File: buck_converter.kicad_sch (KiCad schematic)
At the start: 19 parts, among them Q5 CSD17579Q3A, Q6 CSD17579Q3A, U5 TPS40305DRCR

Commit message: some new ideas for power
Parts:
- removed C47, C53: 1uF, Capacitor_SMD:C_0603_1608Metric_Pad1.08x0.95mm_HandSolder, symbol Device:C
- removed C48: 4.7uF, Capacitor_SMD:C_0603_1608Metric_Pad1.08x0.95mm_HandSolder, symbol Device:C
- removed C49: 3.3nF, Capacitor_SMD:C_0603_1608Metric_Pad1.08x0.95mm_HandSolder, symbol Device:C
- removed C50: 3.9nF, Capacitor_SMD:C_0603_1608Metric_Pad1.08x0.95mm_HandSolder, symbol Device:C
- removed C51: 100pF, Capacitor_SMD:C_0603_1608Metric_Pad1.08x0.95mm_HandSolder, symbol Device:C
- removed C52: 100nF, Capacitor_SMD:C_0603_1608Metric_Pad1.08x0.95mm_HandSolder, symbol Device:C
- removed C54: 1nF, Capacitor_SMD:C_0603_1608Metric_Pad1.08x0.95mm_HandSolder, symbol Device:C
- removed C55: 100uF, Capacitor_SMD:C_0603_1608Metric_Pad1.08x0.95mm_HandSolder, symbol Device:C
- removed L1: XAL7070-182MEC, INDC7275X700N, symbol XAL7070-182MEC:XAL7070-182MEC
- removed Q5, Q6: CSD17579Q3A, Q3A, symbol CSD17579Q3A:CSD17579Q3A
- removed R20: 2k87, Resistor_SMD:R_0603_1608Metric_Pad0.98x0.95mm_HandSolder, symbol Device:R
- removed R21, R24: 10k, Resistor_SMD:R_0603_1608Metric_Pad0.98x0.95mm_HandSolder, symbol Device:R
- removed R22: 100k, Resistor_SMD:R_0603_1608Metric_Pad0.98x0.95mm_HandSolder, symbol Device:R
- removed R23: 249, Resistor_SMD:R_0603_1608Metric_Pad0.98x0.95mm_HandSolder, symbol Device:R
- removed R25: 1k37, Resistor_SMD:R_0603_1608Metric_Pad0.98x0.95mm_HandSolder, symbol Device:R
- removed U5: TPS40305DRCR, Package_SON:Texas_DRC0010J_ThermalVias, symbol New_Library:TPS40305DRCR
- added C56: 16SVPF560M, 16SVPT560M, symbol 16SVPF560M:16SVPF560M
- added C57: 10uF, Capacitor_SMD:C_1210_3225Metric_Pad1.33x2.70mm_HandSolder, symbol Device:C
- added C58: 1uF, Capacitor_SMD:C_0402_1005Metric_Pad0.74x0.62mm_HandSolder, symbol Device:C
- added C59, C60: 100nF, Capacitor_SMD:C_0603_1608Metric_Pad1.08x0.95mm_HandSolder, symbol Device:C
- added C61: 1nF, Capacitor_SMD:C_0402_1005Metric_Pad0.74x0.62mm_HandSolder, symbol Device:C
- added C62: 33pF, Capacitor_SMD:C_0402_1005Metric_Pad0.74x0.62mm_HandSolder, symbol Device:C
- added C63: 1nF, Capacitor_SMD:C_0603_1608Metric_Pad1.08x0.95mm_HandSolder, symbol Device:C
- added C64: 1uF, Capacitor_SMD:C_0603_1608Metric_Pad1.08x0.95mm_HandSolder, symbol Device:C
- added C65, C66, C67: 47uF, Capacitor_SMD:C_1210_3225Metric_Pad1.33x2.70mm_HandSolder, symbol Device:C
- added C68: 16SVPF560M, 16SVPF560M:16SVPT560M, symbol 16SVPF560M:16SVPF560M
- added IC1: TPS55288RPMR, TPS55288RPMR, symbol TPS55288RPMR:TPS55288RPMR
- added L2: XAL7030-272MEC, XAL7030-272MEC:XAL7030272MEC, symbol XAL7030-272MEC:XAL7030-272MEC
- added Q7, Q8: CSD16327Q3, Package_SON:VSON-8_3.3x3.3mm_P0.65mm_NexFET, symbol Transistor_FET:CSD16327Q3
- added R26: 280k, Resistor_SMD:R_0603_1608Metric_Pad0.98x0.95mm_HandSolder, symbol Device:R
- added R27, R33: 100k, Resistor_SMD:R_0603_1608Metric_Pad0.98x0.95mm_HandSolder, symbol Device:R
- added R28, R29: 1, Resistor_SMD:R_0603_1608Metric_Pad0.98x0.95mm_HandSolder, symbol Device:R
- added R30: 49k9, Resistor_SMD:R_0603_1608Metric_Pad0.98x0.95mm_HandSolder, symbol Device:R
- added R31: 33k2, Resistor_SMD:R_0603_1608Metric_Pad0.98x0.95mm_HandSolder, symbol Device:R
- added R32: 287k, Resistor_SMD:R_0603_1608Metric_Pad0.98x0.95mm_HandSolder, symbol Device:R
- added R34: 29k4, Resistor_SMD:R_0603_1608Metric_Pad0.98x0.95mm_HandSolder, symbol Device:R
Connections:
- net +5V: now also C64.1, C65.1, C66.1, C67.1, C68.1 (+), IC1.11 (VOUT_1), IC1.12 (ISP), IC1.13 (ISN_1), IC1.14 (FB/~{INT}), IC1.26 (VOUT_2), IC1.29 (ISN_2), R33.1, R33.2, R34.1
- net GND: now also C56.2 (-), C57.2, C58.2, C62.2, C63.2, C64.2, C65.2, C66.2, C67.2, C68.2 (-), IC1.10 (AGND), IC1.15 (MODE), IC1.24 (PGND_2), IC1.28 (DITH/SYNC_2), IC1.7 (DITH/SYNC_1), IC1.9 (PGND_1), Q8.1 (S), Q8.2 (S), Q8.3 (S), R27.2, R30.2, R31.2, R32.2, R34.2
- new net: IC1.17 (ILIM), R31.1
- new net: C61.2, R32.1
- new net: C61.1, C62.1, IC1.18 (COMP)
- new net: Q7.4 (G), R28.1
- new net: IC1.2 (DR1H), R28.2
- new net: C59.1, IC1.22 (BOOT1), L2.1
- new net: C59.2, IC1.23 (SW1)
- new net: IC1.8 (FSW), R30.1
- new net: IC1.4 (EN/UVLO), R26.2, R27.1
- new net: IC1.1 (DR1L_1), IC1.27 (DR1L_2), R29.2
- new net: C63.1, IC1.19 (VCC_1), IC1.30 (VCC_2)
- new net: C60.2, IC1.20 (BOOT2)
- new net: C60.1, IC1.21 (SW2_1), IC1.25 (SW2_2), L2.2
- new net: Q8.4 (G), R29.1
- new net: Q7.1 (S), Q7.2 (S), Q7.3 (S), Q8.5 (D)
- new net VBUS: C56.1 (+), C57.1, C58.1, IC1.3 (VIN), Q7.5 (D), R26.1
- no-connect marks 0 -> 3
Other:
- note added: "Based on WEBENCH® POWER DESIGNER generations: https://webench.ti.com/appinfo/webench/scripts/SDP.cgi?ID=32A1AC333BF97FA3"
- note removed: "Based on WEBENCH® POWER DESIGNER generations: https://webench.ti.com/appinfo/webench/scripts/SDP.cgi?ID=96FF10E62FAFBBD4"

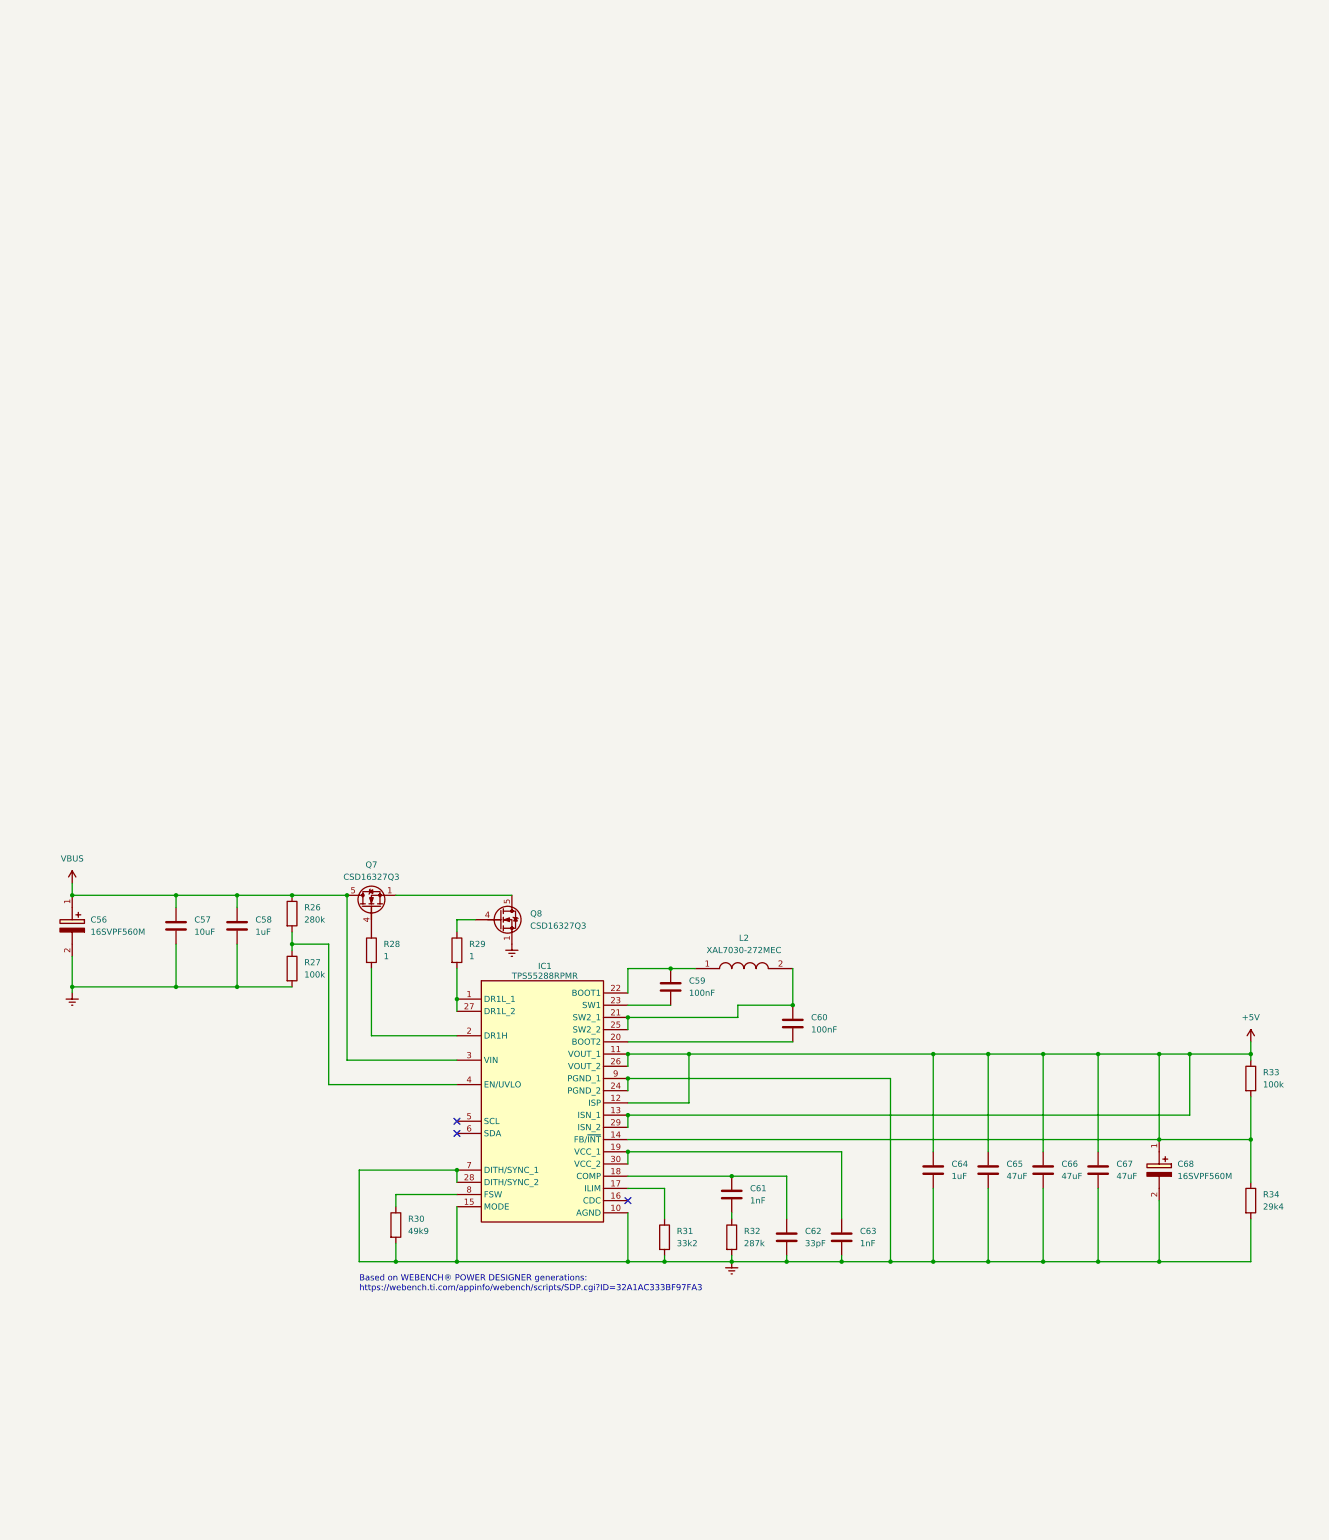
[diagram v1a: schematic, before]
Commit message: started new buck
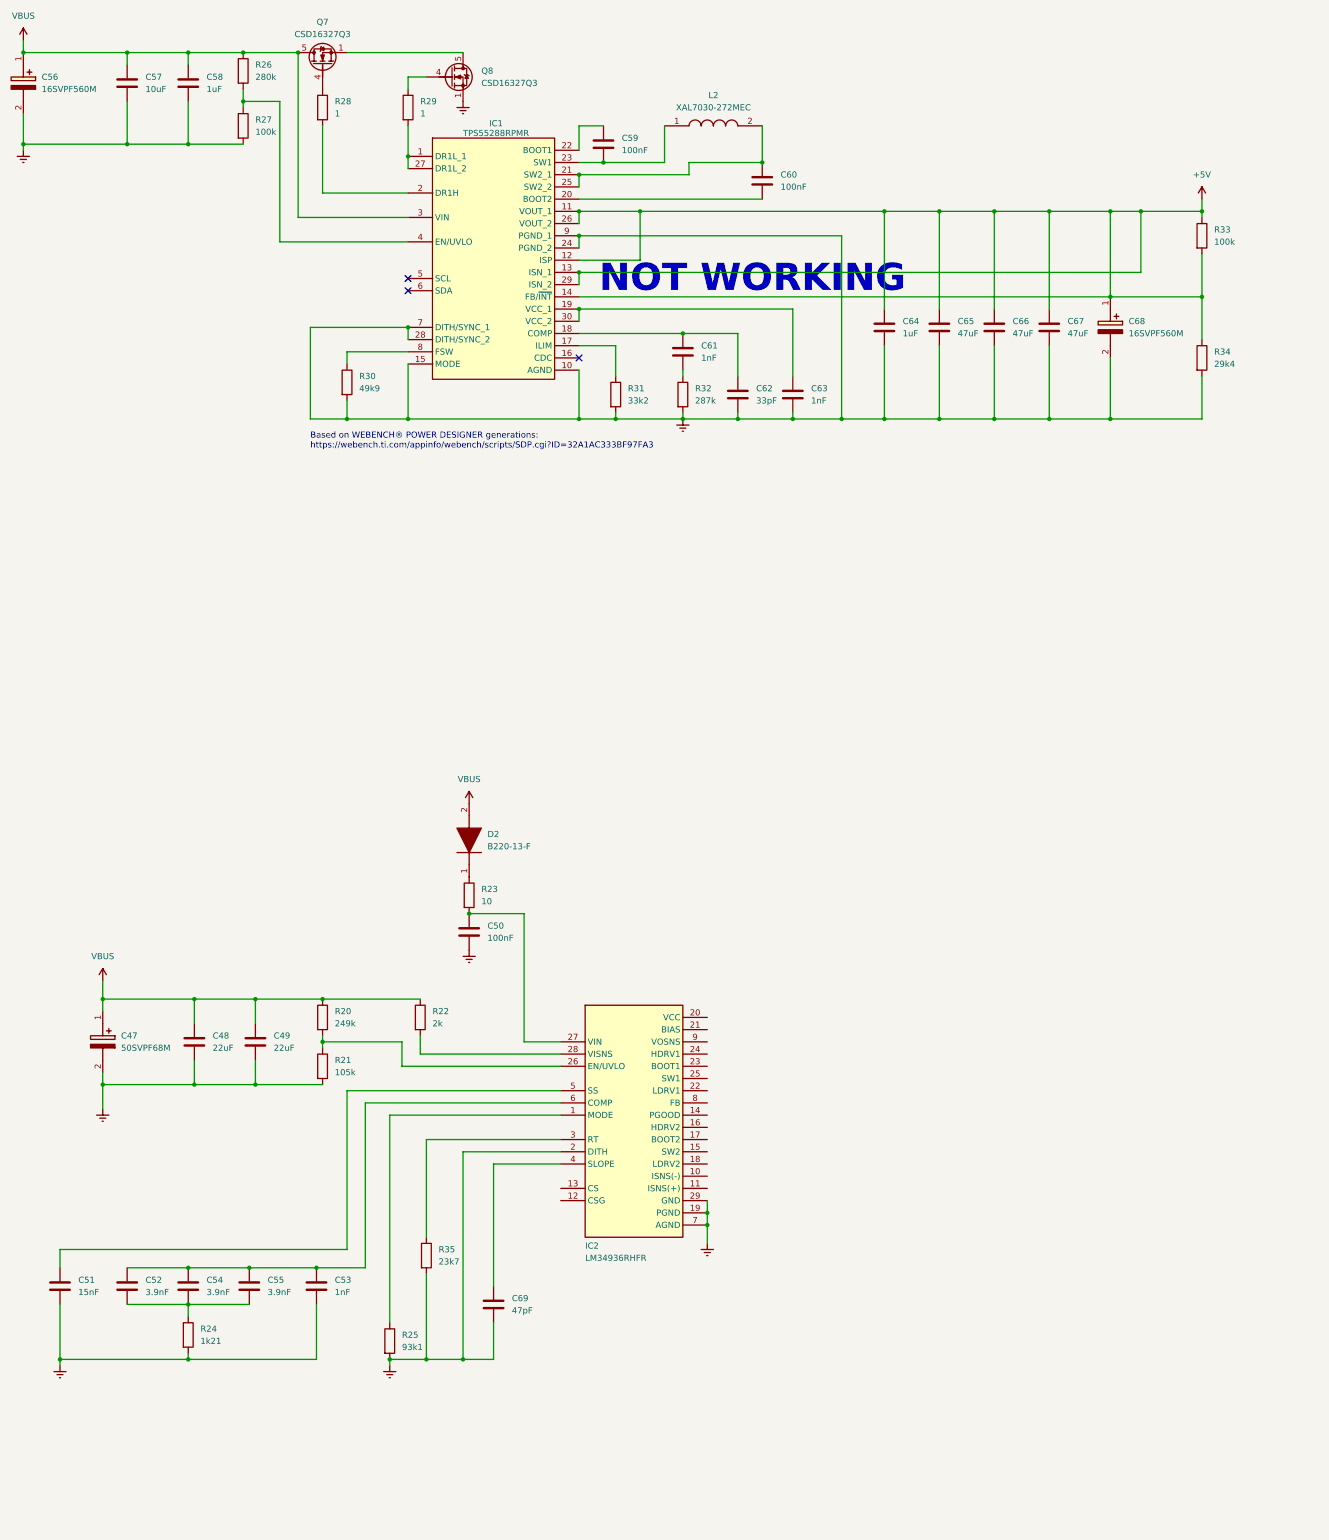
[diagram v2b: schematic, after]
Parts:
- added C47: 50SVPF68M, 50SVPF68M:16SVF1000M, symbol 50SVPF68M:50SVPF68M
- added C48, C49: 22uF, Inductor_SMD:L_1210_3225Metric_Pad1.42x2.65mm_HandSolder, symbol Device:C
- added C50: 100nF, Capacitor_SMD:C_0603_1608Metric_Pad1.08x0.95mm_HandSolder, symbol Device:C
- added C51: 15nF, Capacitor_SMD:C_0603_1608Metric_Pad1.08x0.95mm_HandSolder, symbol Device:C
- added C52, C54, C55: 3.9nF, Capacitor_SMD:C_0805_2012Metric_Pad1.18x1.45mm_HandSolder, symbol Device:C
- added C53: 1nF, Capacitor_SMD:C_0603_1608Metric_Pad1.08x0.95mm_HandSolder, symbol Device:C
- added C69: 47pF, Capacitor_SMD:C_0603_1608Metric_Pad1.08x0.95mm_HandSolder, symbol Device:C
- added D2: B220-13-F, B220-13-F:DIOM5336X250N, symbol B220-13-F:B220-13-F
- added IC2: LM34936RHFR, QFN50P400X500X100-29N-D, symbol LM34936RHFR:LM34936RHFR
- added R20: 249k, Resistor_SMD:R_0603_1608Metric_Pad0.98x0.95mm_HandSolder, symbol Device:R
- added R21: 105k, Resistor_SMD:R_0603_1608Metric_Pad0.98x0.95mm_HandSolder, symbol Device:R
- added R22: 2k, Resistor_SMD:R_0603_1608Metric_Pad0.98x0.95mm_HandSolder, symbol Device:R
- added R23: 10, Resistor_SMD:R_0603_1608Metric_Pad0.98x0.95mm_HandSolder, symbol Device:R
- added R24: 1k21, Resistor_SMD:R_0603_1608Metric_Pad0.98x0.95mm_HandSolder, symbol Device:R
- added R25: 93k1, Resistor_SMD:R_0603_1608Metric_Pad0.98x0.95mm_HandSolder, symbol Device:R
- added R35: 23k7, Resistor_SMD:R_0603_1608Metric_Pad0.98x0.95mm_HandSolder, symbol Device:R
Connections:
- net GND: now also C47.2 (-), C48.2, C49.2, C50.2, C51.2, C53.2, C69.2, IC2.19 (PGND), IC2.2 (DITH), IC2.29 (GND), IC2.7 (AGND), R21.2, R24.2, R25.2, R35.2
- net VBUS: now also C47.1 (+), C48.1, C49.1, D2.2 (A), R20.1, R22.1
- net at C59.1, IC1.22 (BOOT1): no longer L2.1
- net at C59.2, IC1.23 (SW1): now also L2.1
- new net: C52.1, C53.1, C54.1, C55.1, IC2.6 (COMP)
- new net: C52.2, C54.2, C55.2, R24.1
- new net: IC2.26 (EN/UVLO), R20.2, R21.1
- new net: IC2.3 (RT), R35.1
- new net: D2.1 (K), R23.1
- new net: C50.1, IC2.27 (VIN), R23.2
- new net: C51.1, IC2.5 (SS)
- new net: C69.1, IC2.4 (SLOPE)
- new net: IC2.1 (MODE), R25.1
- new net: IC2.28 (VISNS), R22.2
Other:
- note added: "NOT WORKING"
- moved on the sheet: C56, C57, C58, C59, C60, C61, C62, C63, C64, C65, C66, C67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

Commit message: new buck
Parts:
- removed C56: 16SVPF560M, 16SVPT560M, symbol 16SVPF560M:16SVPF560M
- removed C57: 10uF, Capacitor_SMD:C_1210_3225Metric_Pad1.33x2.70mm_HandSolder, symbol Device:C
- removed C58: 1uF, Capacitor_SMD:C_0402_1005Metric_Pad0.74x0.62mm_HandSolder, symbol Device:C
- removed C59, C60: 100nF, Capacitor_SMD:C_0603_1608Metric_Pad1.08x0.95mm_HandSolder, symbol Device:C
- removed C61: 1nF, Capacitor_SMD:C_0402_1005Metric_Pad0.74x0.62mm_HandSolder, symbol Device:C
- removed C62: 33pF, Capacitor_SMD:C_0402_1005Metric_Pad0.74x0.62mm_HandSolder, symbol Device:C
- removed C63: 1nF, Capacitor_SMD:C_0603_1608Metric_Pad1.08x0.95mm_HandSolder, symbol Device:C
- removed C64: 1uF, Capacitor_SMD:C_0603_1608Metric_Pad1.08x0.95mm_HandSolder, symbol Device:C
- removed C65, C66, C67: 47uF, Capacitor_SMD:C_1210_3225Metric_Pad1.33x2.70mm_HandSolder, symbol Device:C
- removed C68: 16SVPF560M, 16SVPF560M:16SVPT560M, symbol 16SVPF560M:16SVPF560M
- removed IC1: TPS55288RPMR, TPS55288RPMR, symbol TPS55288RPMR:TPS55288RPMR
- removed L2: XAL7030-272MEC, XAL7030-272MEC:XAL7030272MEC, symbol XAL7030-272MEC:XAL7030-272MEC
- removed Q7, Q8: CSD16327Q3, Package_SON:VSON-8_3.3x3.3mm_P0.65mm_NexFET, symbol Transistor_FET:CSD16327Q3
- removed R26: 280k, Resistor_SMD:R_0603_1608Metric_Pad0.98x0.95mm_HandSolder, symbol Device:R
- removed R27, R33: 100k, Resistor_SMD:R_0603_1608Metric_Pad0.98x0.95mm_HandSolder, symbol Device:R
- removed R28, R29: 1, Resistor_SMD:R_0603_1608Metric_Pad0.98x0.95mm_HandSolder, symbol Device:R
- removed R30: 49k9, Resistor_SMD:R_0603_1608Metric_Pad0.98x0.95mm_HandSolder, symbol Device:R
- removed R31: 33k2, Resistor_SMD:R_0603_1608Metric_Pad0.98x0.95mm_HandSolder, symbol Device:R
- removed R32: 287k, Resistor_SMD:R_0603_1608Metric_Pad0.98x0.95mm_HandSolder, symbol Device:R
- removed R34: 29k4, Resistor_SMD:R_0603_1608Metric_Pad0.98x0.95mm_HandSolder, symbol Device:R
- added C70: 47pF, Capacitor_SMD:C_0603_1608Metric_Pad1.08x0.95mm_HandSolder, symbol Device:C
- added C71, C72, C73: 100nF, Capacitor_SMD:C_0603_1608Metric_Pad1.08x0.95mm_HandSolder, symbol Device:C
- added C74: 1uF, Capacitor_SMD:C_0603_1608Metric_Pad1.08x0.95mm_HandSolder, symbol Device:C
- added C75, C76, C77: 22uF, Capacitor_SMD:C_0603_1608Metric_Pad1.08x0.95mm_HandSolder, symbol Device:C
- added C78: 47uF, Inductor_SMD:L_1210_3225Metric_Pad1.42x2.65mm_HandSolder, symbol Device:C
- added D4, D5: B220-13-F, DIOM5336X250N, symbol B220-13-F:B220-13-F
- added L1: 74439323010, 74439323010:74439323010, symbol 74439323010:74439323010
- added Q10, Q11, Q6: CSD15571Q2, CSD15571Q2, symbol CSD15571Q2:CSD15571Q2
- added Q5, Q9: CSD17571Q2, CSD25302Q2, symbol CSD17571Q2:CSD17571Q2
- added R36, R37: 100, Resistor_SMD:R_0603_1608Metric_Pad0.98x0.95mm_HandSolder, symbol Device:R
- added R38: 0.01, Resistor_SMD:R_0603_1608Metric_Pad0.98x0.95mm_HandSolder, symbol Device:R
- added R39: 10k, Resistor_SMD:R_0603_1608Metric_Pad0.98x0.95mm_HandSolder, symbol Device:R
- added R40: 105k, Resistor_SMD:R_0603_1608Metric_Pad0.98x0.95mm_HandSolder, symbol Device:R
- added R41: 20k, Resistor_SMD:R_0603_1608Metric_Pad0.98x0.95mm_HandSolder, symbol Device:R
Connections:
- net +5V: now also IC2.9 (VOSNS), C75.1, C76.1, C77.1, C78.1, Q11.1 (D), Q11.2 (D), Q11.5 (D), Q11.6 (D), Q11.7 (D), Q6.1 (D), Q6.2 (D), Q6.5 (D), Q6.6 (D), Q6.7 (D), R40.1
- net GND: now also IC2.10 (ISNS(-)), IC2.11 (ISNS(+)), C71.2, C74.2, C75.2, C76.2, C77.2, C78.2, R36.1, R38.2, R41.2
- net VBUS: now also Q5.1 (D), Q5.2 (D), Q5.5 (D), Q5.6 (D), Q5.8 (D)
- net at IC2.12 (CSG): now also C70.2, R36.2
- net at IC2.13 (CS): now also C70.1, R37.2
- net at IC2.14 (PGOOD): now also R39.1
- net SW2: now reaches IC2.15 (SW2)
- net SW2: now also C73.2, L1.2, Q10.1 (D), Q10.2 (D), Q10.5 (D), Q10.6 (D), Q10.7 (D), Q11.4 (S), Q11.8 (S), Q6.4 (S), Q6.8 (S)
- net at IC2.16 (HDRV2): now also Q11.3 (G), Q6.3 (G)
- net at IC2.17 (BOOT2): now also C73.1, D5.1 (K)
- net at IC2.18 (LDRV2): now also Q10.3 (G)
- net at IC2.20 (VCC): now also C74.1, D4.2 (A), D5.2 (A), R39.2
- net at IC2.21 (BIAS): now also C71.1
- net at IC2.22 (LDRV1): now also Q9.3 (G)
- net at IC2.23 (BOOT1): now also C72.1, D4.1 (K)
- net at IC2.24 (HDRV1): now also Q5.3 (G)
- net SW1: now reaches IC2.25 (SW1)
- net SW1: now also C72.2, L1.1, Q5.4 (S), Q5.7 (S), Q9.1 (D), Q9.2 (D), Q9.5 (D), Q9.6 (D), Q9.8 (D)
- net at IC2.8 (FB): now also R40.2, R41.1
- new net: Q10.4 (S), Q10.8 (S), Q9.4 (S), Q9.7 (S), R37.1, R38.1
- no-connect marks 3 -> 0
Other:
- note added: "Based on WEBENCH® POWER DESIGNER generations: https://webench.ti.com/appinfo/webench/scripts/SDP.cgi?ID=C41C10B83019F89E"
- note removed: "Based on WEBENCH® POWER DESIGNER generations: https://webench.ti.com/appinfo/webench/scripts/SDP.cgi?ID=32A1AC333BF97FA3"
- note removed: "NOT WORKING"
- moved on the sheet: C47, C48, C49, C50, C51, C52, C53, C54, C55, C69, D2, IC2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
